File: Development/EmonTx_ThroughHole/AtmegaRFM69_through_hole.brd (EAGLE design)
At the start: 64.1 x 70 mm, 50 parts, among them CN1 AC 9V, IC1 ATMEGA 328, IC2 MCP1702, J1 1X2-3.5MM, J2 1X2-3.5MM, J3 1X2-3.5MM

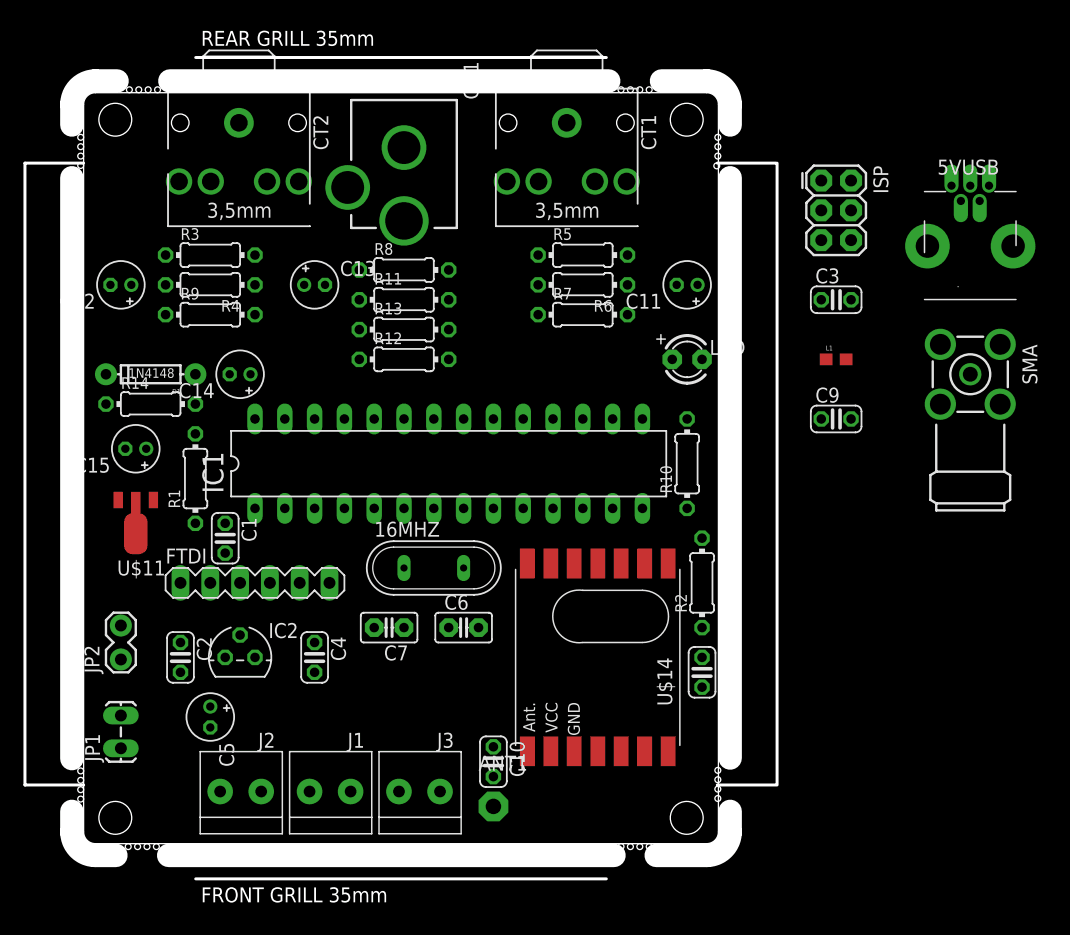
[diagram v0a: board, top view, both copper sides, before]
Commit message: Single voltage regulator, power supply test results, usb positioning
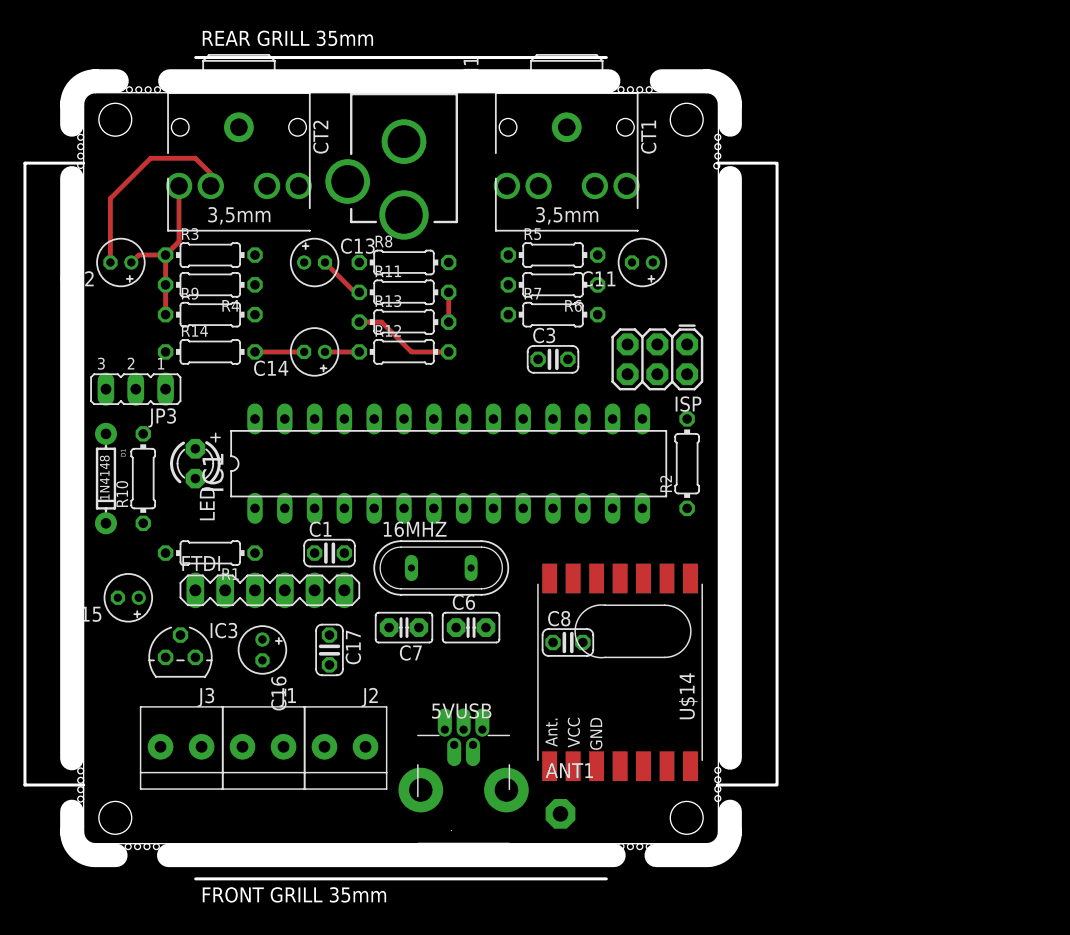
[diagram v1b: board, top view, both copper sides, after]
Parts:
- removed C10, C9: 20pF, resistor:C025-024X044
- removed C2, C4: 0.1µ, resistor:C025-024X044
- removed C5: 10µ, resistor:E1,8-4
- removed IC2: MCP1702, JeeLabs:TO92
- removed JP1: BATT, SparkFun:1X02_LOCK_LONGPADS
- removed JP2: (no value), SparkFun:1X02_LOCK
- removed L1: (no value), SparkFun:0603
- removed SMA: BU-SMA-H, con-coax:BU-SMA-H
- removed U$11: MCP1754, OpenEnergyMonitor:SOT89
- added C16: 10µ, resistor:E1,8-4
- added C17: 0.1µ, resistor:C025-024X044
- added IC3: MCP1702, JeeLabs:TO92
- added JP3: (no value), jumper:JP2
- moved 5VUSB 63.4 mm to (39.4, 1.91)
- moved R10 46.4 mm to (12.1, 33.0)
- moved LED 42.8 mm to (16.5, 34.3), turned to 270 degrees
- moved C3 24.7 mm to (47.0, 43.2)
- moved J3 20.7 mm to (15.2, 10.2)
- moved ISP 18.1 mm to (58.4, 44.5), turned to 180 degrees
- moved C15 12.7 mm to (10.8, 22.9)
- moved C8 11.7 mm to (48.3, 19.1), turned to 0 degrees
- moved R2 10.2 mm to (58.4, 34.3)
- moved J2 9.67 mm to (29.2, 10.2)
- moved D1 9.67 mm to (8.89, 33.0), turned to 270 degrees
- moved C1 8.98 mm to (27.9, 26.7), turned to 0 degrees
- moved J1 6.87 mm to (22.2, 10.2)
- moved R14 6.75 mm to (17.8, 43.8)
- moved C14 6.63 mm to (26.7, 43.8)
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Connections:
- removed net N$11: ANT1.1, C10.2
- removed net N$24: C9.2, SMA.1
- removed net N$6: C15.+, R14.1, U$11.1
- removed net PWR: 5VUSB.VBUS
- new net N$4: C15.+, D1.C, IC3.2
- net 3.3V: now also C16.+, C17.1, IC3.3; no longer C4.1, C5.+, IC2.3, JP1.1, JP2.2
- net 5V: now also 5VUSB.VBUS, JP3.1; no longer C2.1, IC2.2
- net AC: now also R14.2; no longer D1.A
- net AGND: no longer L1.1
- net D4: now also R10.2
- net D9: no longer R10.2
- net DIG1: now also ANT1.1; no longer C10.1, C9.1
- net GND: now also C16.-, C17.2, IC3.1; no longer C2.2, C4.2, C5.-, IC2.1, JP1.2, L1.2, SMA.2, SMA.3, SMA.4, SMA.5, U$11.2, U$11.2.1
- net N$3: now also JP3.3, R14.1; no longer D1.C, R14.2
- net N$5: now also D1.A, JP3.2; no longer JP2.1, U$11.3
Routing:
- net AGND: track 0.00 -> 21.0 mm
- net N$2: track 0.00 -> 14.6 mm
- net ADC0: track 0.00 -> 8.67 mm
- net AC: track 0.00 -> 4.45 mm
- net N$7: track 0.00 -> 2.92 mm
- net N$34: track 0.00 -> 2.54 mm
